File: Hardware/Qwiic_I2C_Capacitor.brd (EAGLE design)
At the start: 21.6 x 7.6 mm, 36 parts, among them J1 CONN_02_0603, J2 QWIIC_RIGHT_ANGLE, J3 PTH, U1 NCD2400MDFN

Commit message: Changes from board review
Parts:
- removed U$10: (no value), buzzard_labels (85):PWR0
- removed U$17, U$2: (no value), buzzard_labels (86):CAP1
- removed U$19: (no value), buzzard_labels (86):I2C0
- added LOGO2: SPECIAL_INSTRUCTIONS-ORDERING, SparkFun-Aesthetics:ORDERING_INSTRUCTIONS
- added R4: 1k, SparkFun-Resistors:0603
- added R5: 10k, SparkFun-Resistors:0402-TIGHT
- added U$11: (no value), buzzard_labels (87):CAP1
- added U$22, U$23: (no value), buzzard_labels (87):DIG0
- U$1: device buzzard_labels (86):I2C0 -> buzzard_labels (88):PWR2
- U$18: device SparkFun-Aesthetics:ORDERING_INSTRUCTIONS -> buzzard_labels (87):CAP1
- moved U$18 58.6 mm to (6.86, 2.03), flipped to the bottom
- moved FRAME1 7.62 mm to (-12.7, -11.4)
- moved U$1 4.44 mm to (13.3, 5.21)
- moved LOGO1 0.76 mm to (4.57, 5.46)
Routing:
- net SCL: vias 3 -> 5
- removed copper zone on layer 1, net GND
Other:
- board text added: "Priyanka Makin"

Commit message: Panelizer/cam output
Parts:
- removed R4: 1k, SparkFun-Resistors:0603
- removed R5: 10k, SparkFun-Resistors:0402-TIGHT
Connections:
- net CN: now also J1.2; no longer J1.P$2
- net CP: now also J1.1; no longer J1.P$1
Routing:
- added copper zone on layer 1, net GND
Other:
- outline, holes or cut-outs redrawn
- board text added: "Route out"
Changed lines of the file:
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@@
 <layer number="27" name="tValues" color="7" fill="1" visible="no" active="yes"/>
 <layer number="28" name="bValues" color="7" fill="1" visible="no" active="yes"/>
-<layer number="29" name="tStop" color="7" fill="3" visible="no" active="yes"/>
-<layer number="30" name="bStop" color="7" fill="6" visible="no" active="yes"/>
+<layer number="29" name="tStop" color="7" fill="3" visible="yes" active="yes"/>
+<layer number="30" name="bStop" color="7" fill="6" visible="yes" active="yes"/>
 <layer number="31" name="tCream" color="7" fill="4" visible="no" active="yes"/>
 <layer number="32" name="bCream" color="7" fill="5" visible="no" active="yes"/>
@@
 <text x="12.7" y="35.56" size="1.778" layer="47" font="vector" ratio="15" align="center">Dimensions in inches</text>
 <text x="35.56" y="39.37" size="1.778" layer="51" font="vector" ratio="15">0.8mm board</text>
-<wire x1="0" y1="0" x2="20.32" y2="0" width="0.1778" layer="20"/>
-<wire x1="20.32" y1="0" x2="20.32" y2="2.54" width="0.1778" layer="20"/>
-<wire x1="20.32" y1="2.54" x2="21.59" y2="2.54" width="0.1778" layer="20"/>
-<wire x1="21.59" y1="2.54" x2="21.59" y2="5.08" width="0.1778" layer="20"/>
-<wire x1="21.59" y1="5.08" x2="20.32" y2="5.08" width="0.1778" layer="20"/>
-<wire x1="20.32" y1="5.08" x2="20.32" y2="7.62" width="0.1778" layer="20"/>
-<wire x1="20.32" y1="7.62" x2="0" y2="7.62" width="0.1778" layer="20"/>
+<wire x1="0" y1="0" x2="20.701" y2="0" width="0.1778" layer="20"/>
+<wire x1="20.701" y1="0" x2="20.701" y2="2.794" width="0.1778" layer="20"/>
+<wire x1="20.701" y1="2.794" x2="21.59" y2="2.794" width="0.1778" layer="20"/>
+<wire x1="21.59" y1="2.794" x2="21.59" y2="4.826" width="0.1778" layer="20"/>
+<wire x1="21.59" y1="4.826" x2="20.701" y2="4.826" width="0.1778" layer="20"/>
+<wire x1="20.701" y1="4.826" x2="20.701" y2="7.62" width="0.1778" layer="20"/>
+<wire x1="20.701" y1="7.62" x2="0" y2="7.62" width="0.1778" layer="20"/>
 <wire x1="0" y1="7.62" x2="0" y2="0" width="0.1778" layer="20"/>
-<rectangle x1="20.828" y1="3.937" x2="21.59" y2="4.699" layer="1"/>
-<rectangle x1="20.828" y1="2.921" x2="21.59" y2="3.683" layer="1"/>
-<rectangle x1="20.828" y1="3.937" x2="21.59" y2="4.699" layer="16"/>
-<rectangle x1="20.828" y1="2.921" x2="21.59" y2="3.683" layer="16"/>
-<rectangle x1="20.828" y1="3.937" x2="21.59" y2="4.699" layer="29"/>
-<rectangle x1="20.828" y1="2.921" x2="21.59" y2="3.683" layer="29"/>
-<rectangle x1="20.828" y1="3.937" x2="21.59" y2="4.699" layer="30"/>
-<rectangle x1="20.828" y1="2.921" x2="21.59" y2="3.683" layer="30"/>
-<rectangle x1="21.59" y1="2.54" x2="22.86" y2="3.81" layer="30"/>
 <text x="19.05" y="-11.43" size="1.778" layer="51" font="vector" ratio="15">Priyanka Makin</text>
+<text x="21.209" y="5.334" size="0.254" layer="20" font="vector" ratio="15" rot="R90">Route out</text>
+<text x="21.209" y="0.381" size="0.254" layer="20" font="vector" ratio="15" rot="R90">Route out</text>
 </plain>
 <attributes>
@@
 </class>
 </classes>
-<designrules name="SparkFun-2-layer-TIGHT">
+<designrules name="SparkFun-2-layer-TIGHT *">
 <description language="en">&lt;b&gt;SparkFun 2 Layer Design Rule Checks - STANDARD/TIGHT/FAB-LIMIT&lt;/b&gt;
 &lt;p&gt;
@@
 <param name="msMicroVia" value="9.99mm"/>
 <param name="msBlindViaRatio" value="0.5"/>
-<param name="rvPadTop" value="0.25"/>
-<param name="rvPadInner" value="0.25"/>
-<param name="rvPadBottom" value="0.25"/>
+<param name="rvPadTop" value="0"/>
+<param name="rvPadInner" value="0"/>
+<param name="rvPadBottom" value="0"/>
 <param name="rvViaOuter" value="0.25"/>
 <param name="rvViaInner" value="0.25"/>
 <param name="rvMicroViaOuter" value="0.25"/>
 <param name="rvMicroViaInner" value="0.25"/>
-<param name="rlMinPadTop" value="7mil"/>
+<param name="rlMinPadTop" value="0mil"/>
 <param name="rlMaxPadTop" value="20mil"/>
 <param name="rlMinPadInner" value="7mil"/>
 <param name="rlMaxPadInner" value="20mil"/>
-<param name="rlMinPadBottom" value="7mil"/>
+<param name="rlMinPadBottom" value="0mil"/>
 <param name="rlMaxPadBottom" value="20mil"/>
 <param name="rlMinViaOuter" value="7mil"/>
@@
 <element name="U$20" library="Labels" package="QWIIC_COPYRIGHT_SMALL" value="" x="1.27" y="3.81" smashed="yes" rot="MR90"/>
 <element name="U$21" library="Labels" package="QWIIC_COPYRIGHT_SMALL" value="" x="1.27" y="3.81" smashed="yes" rot="MR90"/>
-<element name="R4" library="SparkFun-Resistors" package="0603" value="1k" x="25.4" y="3.81" smashed="yes" rot="R90">
-<attribute name="NAME" x="24.638" y="3.81" size="0.6096" layer="25" font="vector" ratio="20" rot="R90" align="bottom-center"/>
-<attribute name="PROD_ID" value="RES-07856" x="25.4" y="3.81" size="1.778" layer="27" font="vector" ratio="15" rot="R90" display="off"/>
-<attribute name="VALUE" x="26.162" y="3.81" size="0.6096" layer="27" font="vector" ratio="20" rot="R90" align="top-center"/>
-</element>
-<element name="R5" library="SparkFun-Resistors" package="0402-TIGHT" value="10k" x="24.13" y="3.81" smashed="yes" rot="R90">
-<attribute name="NAME" x="23.568" y="3.81" size="0.6096" layer="25" font="vector" ratio="20" rot="R90" align="bottom-center"/>
-<attribute name="PROD_ID" value="RES-14241" x="24.13" y="3.81" size="1.778" layer="27" font="vector" ratio="15" rot="R90" display="off"/>
-<attribute name="VALUE" x="24.692" y="3.81" size="0.6096" layer="27" font="vector" ratio="20" rot="R90" align="top-center"/>
-</element>
 <element name="LOGO2" library="SparkFun-Aesthetics" package="ORDERING_INSTRUCTIONS" value="SPECIAL_INSTRUCTIONS-ORDERING" x="31.75" y="53.34" smashed="yes"/>
 <element name="J1" library="Qwiic_Capacitor" package="0603_CASTELLATED" value="CONN_02_0603" x="21.59" y="3.81" smashed="yes" rot="R90"/>
@@
 <polygon width="0.1778" layer="16" isolate="0.3048">
 <vertex x="0" y="0"/>
-<vertex x="20.32" y="0"/>
-<vertex x="20.32" y="2.54"/>
-<vertex x="21.59" y="2.54"/>
-<vertex x="21.59" y="5.08"/>
-<vertex x="20.32" y="5.08"/>
-<vertex x="20.32" y="7.62"/>
+<vertex x="20.701" y="0"/>
+<vertex x="20.701" y="2.794"/>
+<vertex x="21.59" y="2.794"/>
+<vertex x="21.59" y="4.826"/>
+<vertex x="20.701" y="4.826"/>
+<vertex x="20.701" y="7.62"/>
 <vertex x="0" y="7.62"/>
 </polygon>
-<polygon width="0.1778" layer="16" isolate="0.3048">
+<polygon width="0.1778" layer="1" isolate="0.3048">
 <vertex x="0" y="0"/>
-<vertex x="20.32" y="0"/>
-<vertex x="20.32" y="2.54"/>
-<vertex x="21.59" y="2.54"/>
-<vertex x="21.59" y="5.08"/>
-<vertex x="20.32" y="5.08"/>
-<vertex x="20.32" y="7.62"/>
+<vertex x="20.701" y="0"/>
+<vertex x="20.701" y="2.794"/>
+<vertex x="21.59" y="2.794"/>
+<vertex x="21.59" y="4.826"/>
+<vertex x="20.701" y="4.826"/>
+<vertex x="20.701" y="7.62"/>
 <vertex x="0" y="7.62"/>
 </polygon>
@@
 <signal name="CP">
 <contactref element="U1" pad="2"/>
-<contactref element="J1" pad="P$1"/>
-<wire x1="21.59" y1="3.2766" x2="20.828" y2="3.2766" width="0.1778" layer="1"/>
-<wire x1="20.828" y1="3.2766" x2="20.2946" y2="3.81" width="0.1778" layer="1"/>
-<wire x1="20.2946" y1="3.81" x2="20.1041" y2="3.81" width="0.1778" layer="1"/>
+<contactref element="J1" pad="1"/>
+<wire x1="21.59" y1="3.302" x2="21.082" y2="3.81" width="0.1778" layer="1"/>
+<wire x1="21.082" y1="3.81" x2="20.1041" y2="3.81" width="0.1778" layer="1"/>
 </signal>
 <signal name="CN">
 <contactref element="U1" pad="3"/>
-<contactref element="J1" pad="P$2"/>
-<wire x1="21.59" y1="4.3434" x2="21.463" y2="4.4704" width="0.1778" layer="1"/>
-<wire x1="21.463" y1="4.4704" x2="20.1041" y2="4.4704" width="0.1778" layer="1"/>
+<contactref element="J1" pad="2"/>
+<wire x1="21.59" y1="4.318" x2="21.4376" y2="4.4704" width="0.1778" layer="1"/>
+<wire x1="21.4376" y1="4.4704" x2="20.1041" y2="4.4704" width="0.1778" layer="1"/>
 </signal>
 </signals>

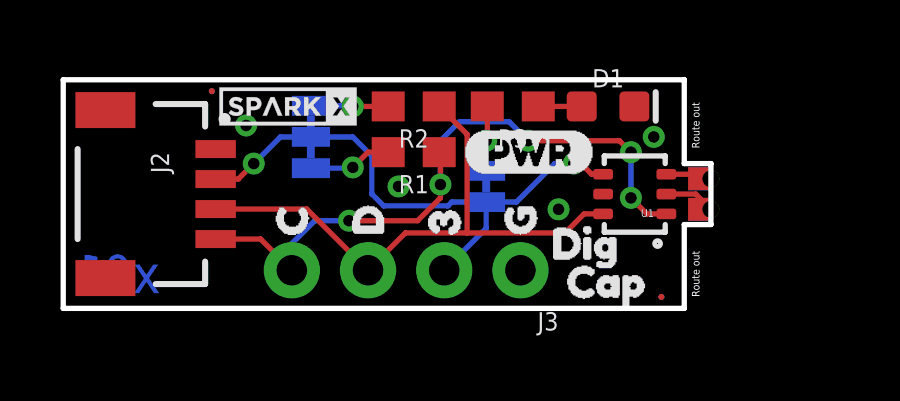
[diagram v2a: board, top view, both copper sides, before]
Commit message: Rev x02
Re-routed SDA and SCL. They were backwards in the previous version x01
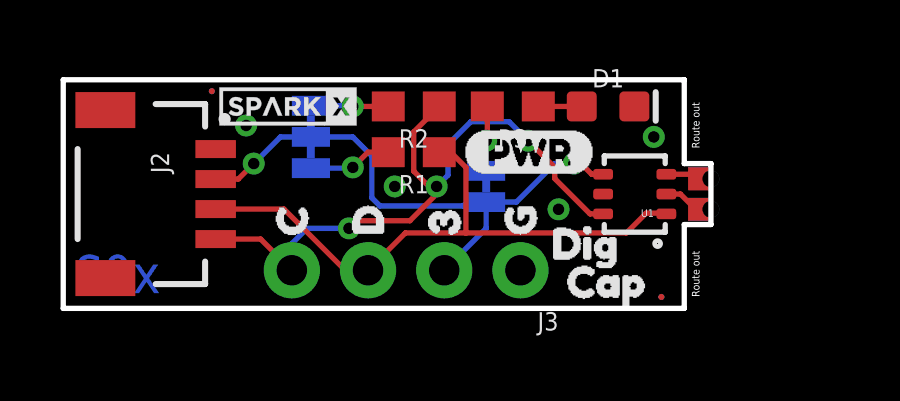
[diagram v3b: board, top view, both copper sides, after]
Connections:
- net SCL: now also R2.1, U1.6; no longer R1.1, U1.1
- net SDA: now also R1.1, U1.1; no longer R2.1, U1.6
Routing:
- net SDA: track 19.1 -> 20.0 mm
- net SCL: track 22.4 -> 21.6 mm, vias 5 -> 3
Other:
- board text added: "x02"
- board text removed: "x01"
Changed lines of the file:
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@@
 <layer number="27" name="tValues" color="7" fill="1" visible="no" active="yes"/>
 <layer number="28" name="bValues" color="7" fill="1" visible="no" active="yes"/>
-<layer number="29" name="tStop" color="7" fill="3" visible="yes" active="yes"/>
-<layer number="30" name="bStop" color="7" fill="6" visible="yes" active="yes"/>
+<layer number="29" name="tStop" color="7" fill="3" visible="no" active="yes"/>
+<layer number="30" name="bStop" color="7" fill="6" visible="no" active="yes"/>
 <layer number="31" name="tCream" color="7" fill="4" visible="no" active="yes"/>
 <layer number="32" name="bCream" color="7" fill="5" visible="no" active="yes"/>
@@
 <board>
 <plain>
-<text x="1.778" y="1.143" size="1.27" layer="16" font="vector" ratio="15" rot="MR0" align="center">x01</text>
+<text x="1.778" y="1.143" size="1.27" layer="16" font="vector" ratio="15" rot="MR0" align="center">x02</text>
 <dimension x1="0" y1="0" x2="0" y2="25.4" x3="-5.08" y3="12.7" textsize="1.778" textratio="15" layer="47" unit="inch"/>
 <dimension x1="2.54" y1="22.86" x2="2.54" y2="0" x3="-1.27" y3="11.43" textsize="1.778" textratio="15" layer="47" unit="inch"/>
@@
 <wire x1="17.018" y1="4.826" x2="17.2593" y2="4.826" width="0.1778" layer="1"/>
 <wire x1="17.6149" y1="4.4704" x2="17.9959" y2="4.4704" width="0.1778" layer="1"/>
-<wire x1="10.287" y1="3.81" x2="10.287" y2="5.08" width="0.1778" layer="16"/>
+<wire x1="10.287" y1="3.683" x2="10.287" y2="5.08" width="0.1778" layer="16"/>
 <wire x1="10.287" y1="5.08" x2="9.652" y2="5.715" width="0.1778" layer="16"/>
-<wire x1="14.097" y1="3.5433" x2="12.954" y2="3.5433" width="0.1778" layer="16"/>
-<wire x1="12.954" y1="3.5433" x2="12.827" y2="3.4163" width="0.1778" layer="16"/>
-<wire x1="12.827" y1="3.4163" x2="10.6807" y2="3.4163" width="0.1778" layer="16"/>
-<wire x1="10.6807" y1="3.4163" x2="10.287" y2="3.81" width="0.1778" layer="16"/>
+<wire x1="14.097" y1="3.5433" x2="13.462" y2="3.5433" width="0.1778" layer="16"/>
+<wire x1="13.462" y1="3.5433" x2="13.335" y2="3.4163" width="0.1778" layer="16"/>
+<wire x1="13.335" y1="3.4163" x2="10.5537" y2="3.4163" width="0.1778" layer="16"/>
+<wire x1="10.5537" y1="3.4163" x2="10.287" y2="3.683" width="0.1778" layer="16"/>
 <wire x1="9.652" y1="5.715" x2="8.255" y2="5.715" width="0.1778" layer="16"/>
 </signal>
@@
 <via x="19.685" y="5.715" extent="1-16" drill="0.381"/>
 <via x="16.51" y="3.302" extent="1-16" drill="0.381"/>
-<via x="11.176" y="4.064" extent="1-16" drill="0.381"/>
-<polygon width="0.1778" layer="16" isolate="0.3048">
+<polygon width="0.1778" layer="16" isolate="0.2032">
 <vertex x="0" y="0"/>
 <vertex x="20.701" y="0"/>
@@
 <vertex x="0" y="7.62"/>
 </polygon>
-<polygon width="0.1778" layer="1" isolate="0.3048">
+<polygon width="0.1778" layer="1" isolate="0.2032">
 <vertex x="0" y="0"/>
 <vertex x="20.701" y="0"/>
@@
 <vertex x="0" y="7.62"/>
 </polygon>
+<via x="11.049" y="4.064" extent="1-16" drill="0.381"/>
 </signal>
 <signal name="SCL">
 <contactref element="J2" pad="4"/>
 <contactref element="J3" pad="4"/>
-<contactref element="U1" pad="1"/>
-<contactref element="R1" pad="1"/>
 <wire x1="5.08" y1="2.31" x2="6.58" y2="2.31" width="0.1778" layer="1"/>
 <wire x1="6.58" y1="2.31" x2="7.62" y2="1.27" width="0.1778" layer="1"/>
 <wire x1="7.62" y1="1.27" x2="7.62" y2="2.159" width="0.1778" layer="16"/>
-<wire x1="8.382" y1="2.921" x2="9.525" y2="2.921" width="0.1778" layer="16"/>
-<via x="9.525" y="2.921" extent="1-16" drill="0.381"/>
-<wire x1="12.534" y1="5.207" x2="12.573" y2="5.168" width="0.1778" layer="1"/>
-<wire x1="12.573" y1="5.168" x2="12.573" y2="4.1275" width="0.1778" layer="1"/>
-<wire x1="12.573" y1="4.1275" x2="12.573" y2="3.683" width="0.1778" layer="1"/>
-<wire x1="12.573" y1="3.683" x2="11.811" y2="2.921" width="0.1778" layer="1"/>
-<wire x1="11.811" y1="2.921" x2="9.525" y2="2.921" width="0.1778" layer="1"/>
-<wire x1="7.62" y1="2.159" x2="8.382" y2="2.921" width="0.1778" layer="16"/>
-<wire x1="20.1041" y1="3.1496" x2="19.4564" y2="3.1496" width="0.1778" layer="1"/>
-<wire x1="18.923" y1="3.683" x2="18.923" y2="5.207" width="0.1778" layer="16"/>
-<wire x1="18.923" y1="5.207" x2="18.542" y2="5.588" width="0.1778" layer="1"/>
-<wire x1="18.542" y1="5.588" x2="15.494" y2="5.588" width="0.1778" layer="1"/>
-<wire x1="19.4564" y1="3.1496" x2="18.923" y2="3.683" width="0.1778" layer="1"/>
+<wire x1="8.128" y1="2.667" x2="9.525" y2="2.667" width="0.1778" layer="16"/>
+<via x="9.525" y="2.667" extent="1-16" drill="0.381"/>
+<wire x1="7.62" y1="2.159" x2="8.128" y2="2.667" width="0.1778" layer="16"/>
 <via x="15.494" y="5.588" extent="1-16" drill="0.381"/>
 <wire x1="15.494" y1="5.588" x2="14.859" y2="6.223" width="0.1778" layer="16"/>
-<wire x1="14.859" y1="6.223" x2="13.208" y2="6.223" width="0.1778" layer="16"/>
-<wire x1="13.208" y1="6.223" x2="12.573" y2="5.588" width="0.1778" layer="16"/>
-<wire x1="12.573" y1="5.588" x2="12.573" y2="4.1275" width="0.1778" layer="16"/>
-<via x="12.573" y="4.1275" extent="1-16" drill="0.381"/>
-<via x="18.923" y="3.683" extent="1-16" drill="0.381"/>
-<via x="18.923" y="5.207" extent="1-16" drill="0.381"/>
+<wire x1="14.859" y1="6.223" x2="13.589" y2="6.223" width="0.1778" layer="16"/>
+<wire x1="13.589" y1="6.223" x2="12.827" y2="5.461" width="0.1778" layer="16"/>
+<contactref element="U1" pad="6"/>
+<contactref element="R2" pad="1"/>
+<wire x1="15.494" y1="5.588" x2="16.383" y2="4.699" width="0.1778" layer="1"/>
+<wire x1="16.383" y1="4.699" x2="16.383" y2="4.32703125" width="0.1778" layer="1"/>
+<wire x1="16.383" y1="4.32703125" x2="17.56043125" y2="3.1496" width="0.1778" layer="1"/>
+<wire x1="17.56043125" y1="3.1496" x2="17.9959" y2="3.1496" width="0.1778" layer="1"/>
+<wire x1="11.557" y1="2.921" x2="9.779" y2="2.921" width="0.1778" layer="1"/>
+<wire x1="9.525" y1="2.667" x2="9.779" y2="2.921" width="0.1778" layer="1"/>
+<wire x1="11.684" y1="5.881" x2="12.534" y2="6.731" width="0.1778" layer="1"/>
+<wire x1="12.446" y1="3.81" x2="11.557" y2="2.921" width="0.1778" layer="1"/>
+<wire x1="12.446" y1="3.81" x2="12.446" y2="4.064" width="0.1778" layer="1"/>
+<wire x1="11.684" y1="5.881" x2="11.684" y2="4.572" width="0.1778" layer="1"/>
+<wire x1="12.446" y1="4.064" x2="12.192" y2="4.064" width="0.1778" layer="1"/>
+<wire x1="12.192" y1="4.064" x2="11.684" y2="4.572" width="0.1778" layer="1"/>
+<wire x1="12.827" y1="5.461" x2="12.827" y2="4.445" width="0.1778" layer="16"/>
+<wire x1="12.827" y1="4.445" x2="12.446" y2="4.064" width="0.1778" layer="16"/>
+<via x="12.446" y="4.064" extent="1-16" drill="0.381"/>
 </signal>
 <signal name="SDA">
 <contactref element="J2" pad="3"/>
 <contactref element="J3" pad="3"/>
-<contactref element="U1" pad="6"/>
-<contactref element="R2" pad="1"/>
-<wire x1="5.08" y1="3.31" x2="8.12" y2="3.31" width="0.1778" layer="1"/>
-<wire x1="8.12" y1="3.31" x2="10.16" y2="1.27" width="0.1778" layer="1"/>
-<wire x1="12.534" y1="6.731" x2="13.462" y2="5.803" width="0.1778" layer="1"/>
-<wire x1="16.7259" y1="2.5146" x2="13.462" y2="2.5146" width="0.1778" layer="1"/>
-<wire x1="13.462" y1="2.5146" x2="11.4046" y2="2.5146" width="0.1778" layer="1"/>
+<wire x1="5.08" y1="3.31" x2="7.358" y2="3.31" width="0.1778" layer="1"/>
+<wire x1="9.398" y1="1.27" x2="10.16" y2="1.27" width="0.1778" layer="1"/>
+<wire x1="9.398" y1="1.27" x2="7.358" y2="3.31" width="0.1778" layer="1"/>
+<wire x1="13.423" y1="2.5146" x2="11.4046" y2="2.5146" width="0.1778" layer="1"/>
 <wire x1="11.4046" y1="2.5146" x2="10.16" y2="1.27" width="0.1778" layer="1"/>
-<wire x1="17.9959" y1="3.1496" x2="17.3609" y2="3.1496" width="0.1778" layer="1"/>
-<wire x1="17.3609" y1="3.1496" x2="16.7259" y2="2.5146" width="0.1778" layer="1"/>
-<wire x1="13.462" y1="5.803" x2="13.462" y2="2.5146" width="0.1778" layer="1"/>
+<contactref element="U1" pad="1"/>
+<contactref element="R1" pad="1"/>
+<wire x1="18.7706" y1="2.5146" x2="19.431" y2="3.175" width="0.1778" layer="1"/>
+<wire x1="19.431" y1="3.175" x2="20.0787" y2="3.175" width="0.1778" layer="1"/>
+<wire x1="20.0787" y1="3.175" x2="20.1041" y2="3.1496" width="0.1778" layer="1"/>
+<wire x1="13.423" y1="2.5146" x2="18.7706" y2="2.5146" width="0.1778" layer="1"/>
+<wire x1="12.534" y1="5.207" x2="12.915" y2="5.207" width="0.1778" layer="1"/>
+<wire x1="13.423" y1="4.699" x2="12.915" y2="5.207" width="0.1778" layer="1"/>
+<wire x1="13.423" y1="4.699" x2="13.423" y2="2.5146" width="0.1778" layer="1"/>
 </signal>
 <signal name="N$3">
@@
 <contactref element="U1" pad="2"/>
 <contactref element="J1" pad="1"/>
-<wire x1="21.59" y1="3.302" x2="21.082" y2="3.81" width="0.1778" layer="1"/>
-<wire x1="21.082" y1="3.81" x2="20.1041" y2="3.81" width="0.1778" layer="1"/>
+<wire x1="21.59" y1="3.302" x2="21.082" y2="3.302" width="0.1778" layer="1"/>
+<wire x1="21.082" y1="3.302" x2="20.574" y2="3.81" width="0.1778" layer="1"/>
+<wire x1="20.574" y1="3.81" x2="20.1041" y2="3.81" width="0.1778" layer="1"/>
 </signal>
 <signal name="CN">
